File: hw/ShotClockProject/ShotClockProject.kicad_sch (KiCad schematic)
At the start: 8 parts, among them SW1 TK-6580S-1

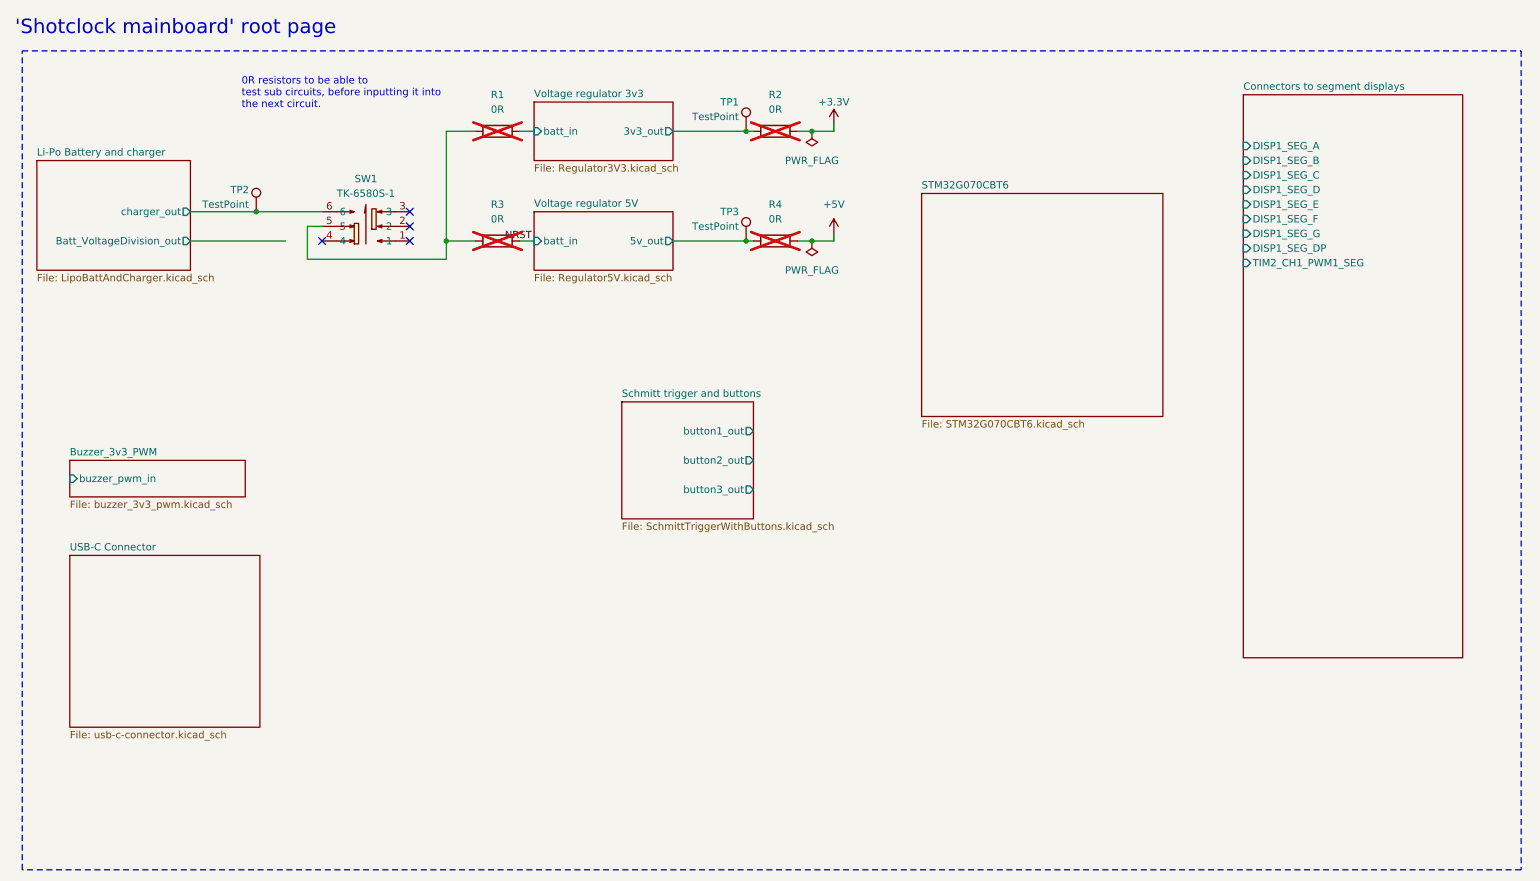
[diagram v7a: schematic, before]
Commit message: Added I2C support
Calculated pull-up resistor values
Added 6 pin female headers to mainboard
Added nRESET line for the I2C chips
Removed PCB routing and part placement
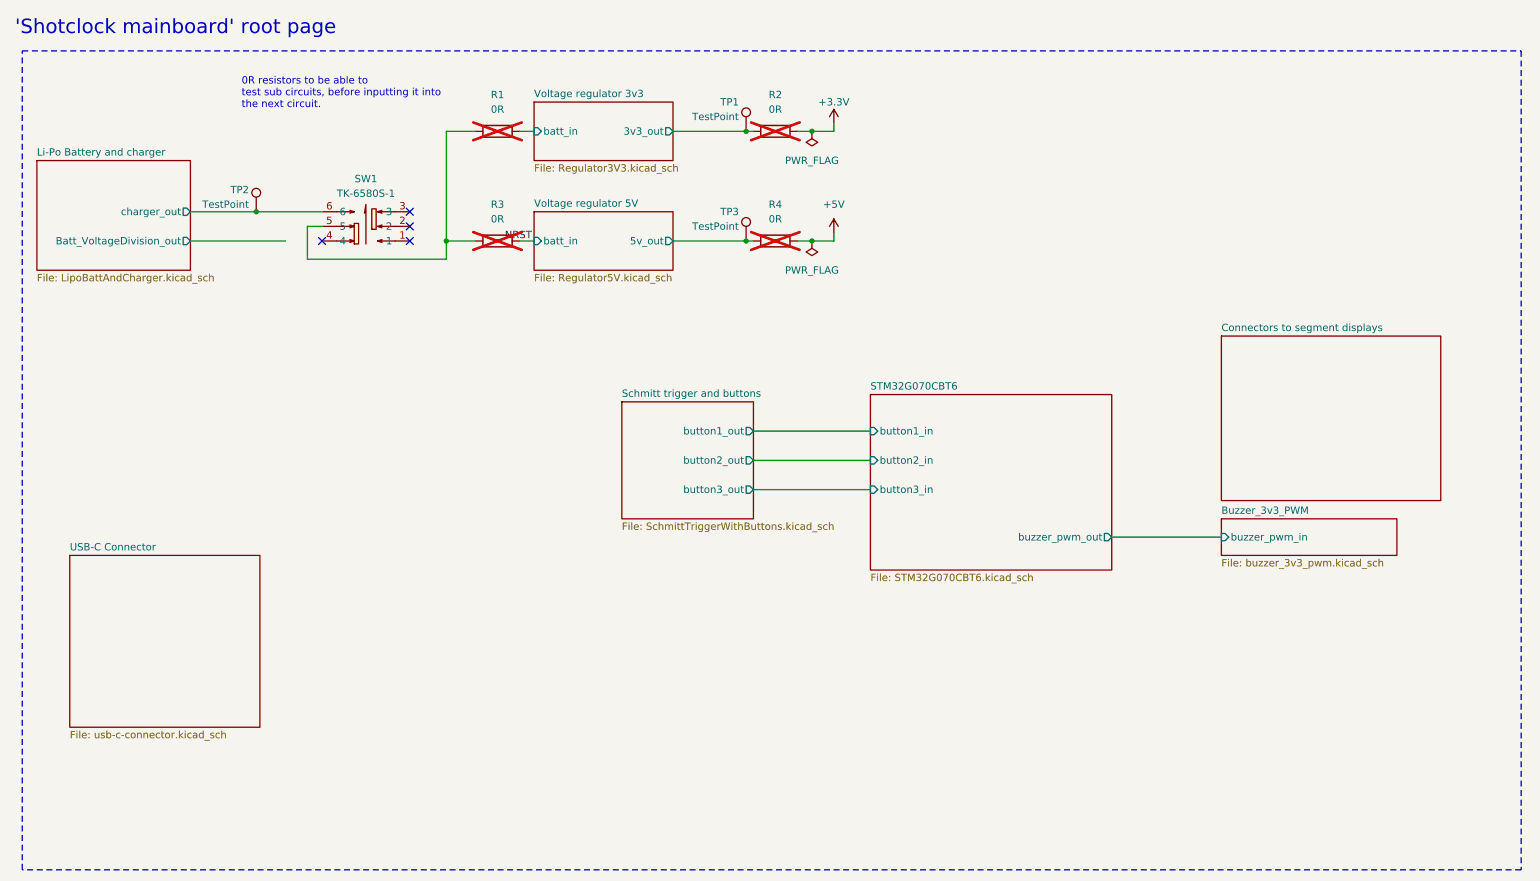
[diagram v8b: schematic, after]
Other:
- sheet Connectors to segment displays ports: added none; removed DISP1_SEG_A, DISP1_SEG_B, DISP1_SEG_C, DISP1_SEG_D, DISP1_SEG_DP, DISP1_SEG_E, DISP1_SEG_F, DISP1_SEG_G, TIM2_CH1_PWM1_SEG
- sheet STM32G070CBT6 ports: added button1_in, button2_in, button3_in, buzzer_pwm_out; removed none
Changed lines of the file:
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@@
+    (stroke (width 0) (type default))
+  )
+  (wire (pts (xy 208.28 106.045) (xy 227.33 106.045))
     (stroke (width 0) (type default))
   )
@@
     (stroke (width 0) (type default))
   )
+  (wire (pts (xy 146.05 87.63) (xy 166.37 87.63))
+    (stroke (width 0) (type default))
+  )
   (wire (pts (xy 160.02 35.56) (xy 160.02 34.29))
     (stroke (width 0) (type default))
@@
     (stroke (width 0) (type default))
   )
+  (wire (pts (xy 146.05 92.71) (xy 166.37 92.71))
+    (stroke (width 0) (type default))
+  )
   (wire (pts (xy 156.21 35.56) (xy 160.02 35.56))
     (stroke (width 0) (type default))
   )
   (wire (pts (xy 105.41 54.61) (xy 107.95 54.61))
+    (stroke (width 0) (type default))
+  )
+  (wire (pts (xy 146.05 97.79) (xy 166.37 97.79))
     (stroke (width 0) (type default))
   )
@@
     )
   )
-  (sheet (at 27.305 92.71) (size 30.48 6.35) (fields_autoplaced)
-    (stroke (width 0.1524) (type solid))
-    (fill (color 0 0 0 0.0000))
-    (property "Sheetname" "Buzzer_3v3_PWM" (at 27.305 91.9984 0)
-      (effects (font (size 1.27 1.27)) (justify left bottom))
-    )
-    (property "Sheetfile" "buzzer_3v3_pwm.kicad_sch" (at 27.305 99.6446 0)
+  (sheet (at 227.33 102.87) (size 30.48 6.35) (fields_autoplaced)
+    (stroke (width 0.1524) (type solid))
+    (fill (color 0 0 0 0.0000))
+    (property "Sheetname" "Buzzer_3v3_PWM" (at 227.33 102.1584 0)
+      (effects (font (size 1.27 1.27)) (justify left bottom))
+    )
+    (property "Sheetfile" "buzzer_3v3_pwm.kicad_sch" (at 227.33 109.8046 0)
       (effects (font (size 1.27 1.27)) (justify left top))
     )
-    (pin "buzzer_pwm_in" input (at 27.305 95.885 180)
-      (effects (font (size 1.27 1.27)) (justify left))
-    )
-    (instances
-      (project "ShotClockProject"
-        (path "/5fd859aa-754d-49c2-9762-3f7ebe3bb64c" (page "8"))
+    (pin "buzzer_pwm_in" input (at 227.33 106.045 180)
+      (effects (font (size 1.27 1.27)) (justify left))
+    )
+    (instances
+      (project "ShotClockProject"
+        (path "/5fd859aa-754d-49c2-9762-3f7ebe3bb64c" (page "7"))
       )
     )
@@
     (instances
       (project "ShotClockProject"
-        (path "/5fd859aa-754d-49c2-9762-3f7ebe3bb64c" (page "4"))
+        (path "/5fd859aa-754d-49c2-9762-3f7ebe3bb64c" (page "3"))
       )
     )
@@
     (instances
       (project "ShotClockProject"
-        (path "/5fd859aa-754d-49c2-9762-3f7ebe3bb64c" (page "6"))
-      )
-    )
-  )
-  (sheet (at 175.26 46.355) (size 41.91 38.735) (fields_autoplaced)
-    (stroke (width 0.1524) (type solid))
-    (fill (color 0 0 0 0.0000))
-    (property "Sheetname" "STM32G070CBT6" (at 175.26 45.6434 0)
-      (effects (font (size 1.27 1.27)) (justify left bottom))
-    )
-    (property "Sheetfile" "STM32G070CBT6.kicad_sch" (at 175.26 85.6746 0)
+        (path "/5fd859aa-754d-49c2-9762-3f7ebe3bb64c" (page "5"))
+      )
+    )
+  )
+  (sheet (at 166.37 81.28) (size 41.91 30.48) (fields_autoplaced)
+    (stroke (width 0.1524) (type solid))
+    (fill (color 0 0 0 0.0000))
+    (property "Sheetname" "STM32G070CBT6" (at 166.37 80.5684 0)
+      (effects (font (size 1.27 1.27)) (justify left bottom))
+    )
+    (property "Sheetfile" "STM32G070CBT6.kicad_sch" (at 166.37 112.3446 0)
       (effects (font (size 1.27 1.27)) (justify left top))
     )
-    (instances
-      (project "ShotClockProject"
-        (path "/5fd859aa-754d-49c2-9762-3f7ebe3bb64c" (page "10"))
+    (pin "button3_in" input (at 166.37 97.79 180)
+      (effects (font (size 1.27 1.27)) (justify left))
+    )
+    (pin "button1_in" input (at 166.37 87.63 180)
+      (effects (font (size 1.27 1.27)) (justify left))
+    )
+    (pin "button2_in" input (at 166.37 92.71 180)
+      (effects (font (size 1.27 1.27)) (justify left))
+    )
+    (pin "buzzer_pwm_out" output (at 208.28 106.045 0)
+      (effects (font (size 1.27 1.27)) (justify right))
+    )
+    (instances
+      (project "ShotClockProject"
+        (path "/5fd859aa-754d-49c2-9762-3f7ebe3bb64c" (page "1"))
       )
     )
@@
     (instances
       (project "ShotClockProject"
-        (path "/5fd859aa-754d-49c2-9762-3f7ebe3bb64c" (page "5"))
+        (path "/5fd859aa-754d-49c2-9762-3f7ebe3bb64c" (page "4"))
       )
     )
@@
     (instances
       (project "ShotClockProject"
-        (path "/5fd859aa-754d-49c2-9762-3f7ebe3bb64c" (page "9"))
+        (path "/5fd859aa-754d-49c2-9762-3f7ebe3bb64c" (page "8"))
       )
     )
@@
     (instances
       (project "ShotClockProject"
-        (path "/5fd859aa-754d-49c2-9762-3f7ebe3bb64c" (page "3"))
-      )
-    )
-  )
-  (sheet (at 231.14 29.21) (size 38.1 97.79) (fields_autoplaced)
-    (stroke (width 0.1524) (type solid))
-    (fill (color 0 0 0 0.0000))
-    (property "Sheetname" "Connectors to segment displays" (at 231.14 28.4984 0)
-      (effects (font (size 1.27 1.27)) (justify left bottom))
-    )
-    (property "Sheetfile" "header_connectors_segment.kicad_sch" (at 231.14 127.5846 0)
+        (path "/5fd859aa-754d-49c2-9762-3f7ebe3bb64c" (page "2"))
+      )
+    )
+  )
+  (sheet (at 227.33 71.12) (size 38.1 28.575) (fields_autoplaced)
+    (stroke (width 0.1524) (type solid))
+    (fill (color 0 0 0 0.0000))
+    (property "Sheetname" "Connectors to segment displays" (at 227.33 70.4084 0)
+      (effects (font (size 1.27 1.27)) (justify left bottom))
+    )
+    (property "Sheetfile" "header_connectors_segment.kicad_sch" (at 227.33 100.2796 0)
       (effects (font (size 1.27 1.27)) (justify left top) hide)
     )
-    (pin "DISP1_SEG_DP" input (at 231.14 55.88 180)
-      (effects (font (size 1.27 1.27)) (justify left))
-    )
-    (pin "DISP1_SEG_F" input (at 231.14 50.8 180)
-      (effects (font (size 1.27 1.27)) (justify left))
-    )
-    (pin "DISP1_SEG_B" input (at 231.14 40.64 180)
-      (effects (font (size 1.27 1.27)) (justify left))
-    )
-    (pin "DISP1_SEG_D" input (at 231.14 45.72 180)
-      (effects (font (size 1.27 1.27)) (justify left))
-    )
-    (pin "DISP1_SEG_C" input (at 231.14 43.18 180)
-      (effects (font (size 1.27 1.27)) (justify left))
-    )
-    (pin "DISP1_SEG_E" input (at 231.14 48.26 180)
-      (effects (font (size 1.27 1.27)) (justify left))
-    )
-    (pin "TIM2_CH1_PWM1_SEG" input (at 231.14 58.42 180)
-      (effects (font (size 1.27 1.27)) (justify left))
-    )
-    (pin "DISP1_SEG_G" input (at 231.14 53.34 180)
-      (effects (font (size 1.27 1.27)) (justify left))
-    )
-    (pin "DISP1_SEG_A" input (at 231.14 38.1 180)
-      (effects (font (size 1.27 1.27)) (justify left))
-    )
-    (instances
-      (project "ShotClockProject"
-        (path "/5fd859aa-754d-49c2-9762-3f7ebe3bb64c" (page "7"))
-      )
-    )
+    (instances
+      (project "ShotClockProject"
+        (path "/5fd859aa-754d-49c2-9762-3f7ebe3bb64c" (page "6"))
+      )
+    )
